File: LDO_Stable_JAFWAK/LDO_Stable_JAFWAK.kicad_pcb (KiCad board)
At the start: 4 copper layers, 96.5 x 50.8 mm, 76 parts, among them J1 VIN_DC, J12 EN_FG, J15 VOUT_BUFF, J16 VDD_SEL, J17 VS_BUFF, J18 EN_SEL, J2 VOUT, J24 Load Cell and Buffer, J3 GND, J4 GND, J5 EN_AIN_SEL, J6 AD_PINS, J8 VIN_FG, Q10 FDV305N, Q6 FDV305N, Q7 FDV305N, Q8 FDV305N, Q9 FDV305N, U1 SU272AFJK_LDO, U2 TMP235A2DBZR, U5 BUF634AIDR, U6 FXLP34, U7 BUF634AIDR, U8 FXLP34

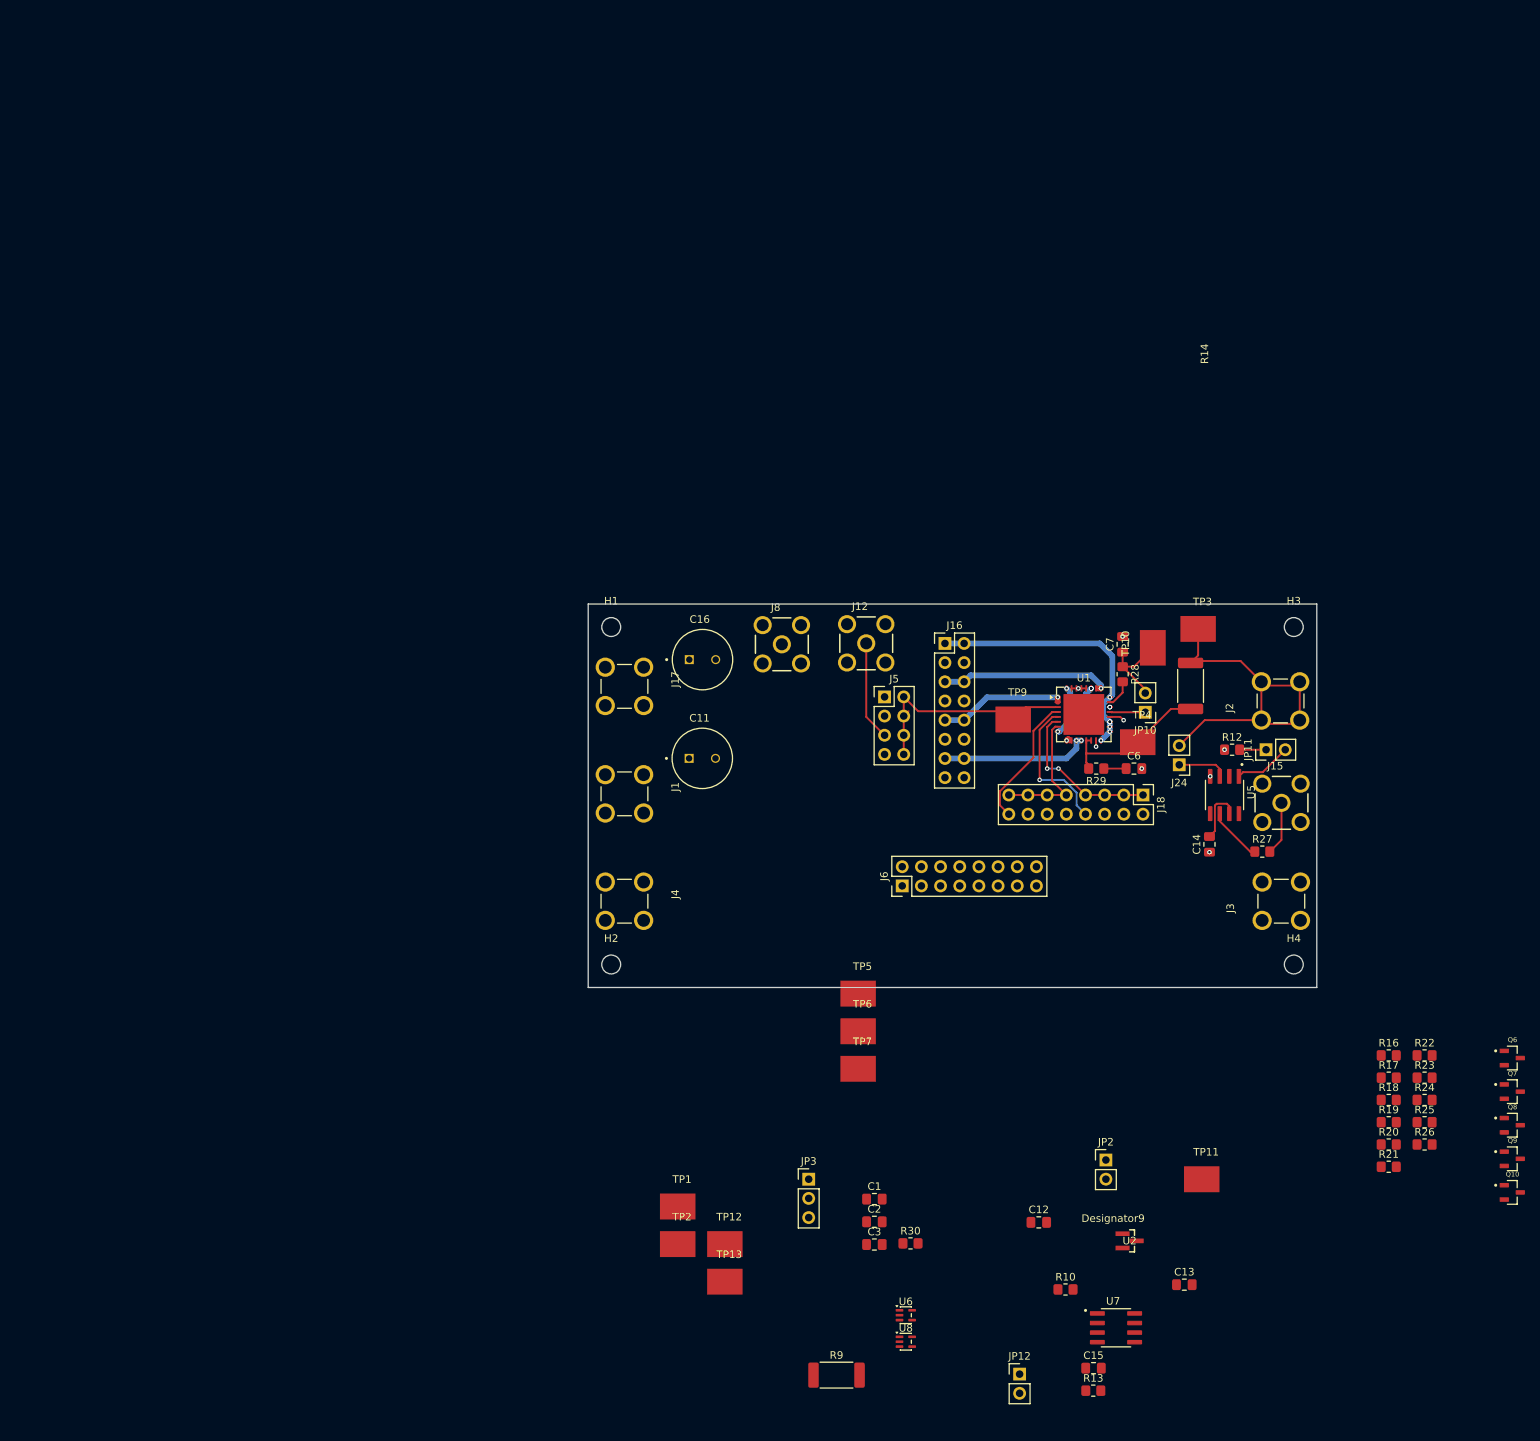
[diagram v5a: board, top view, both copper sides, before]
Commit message: Update PCB placement and routing
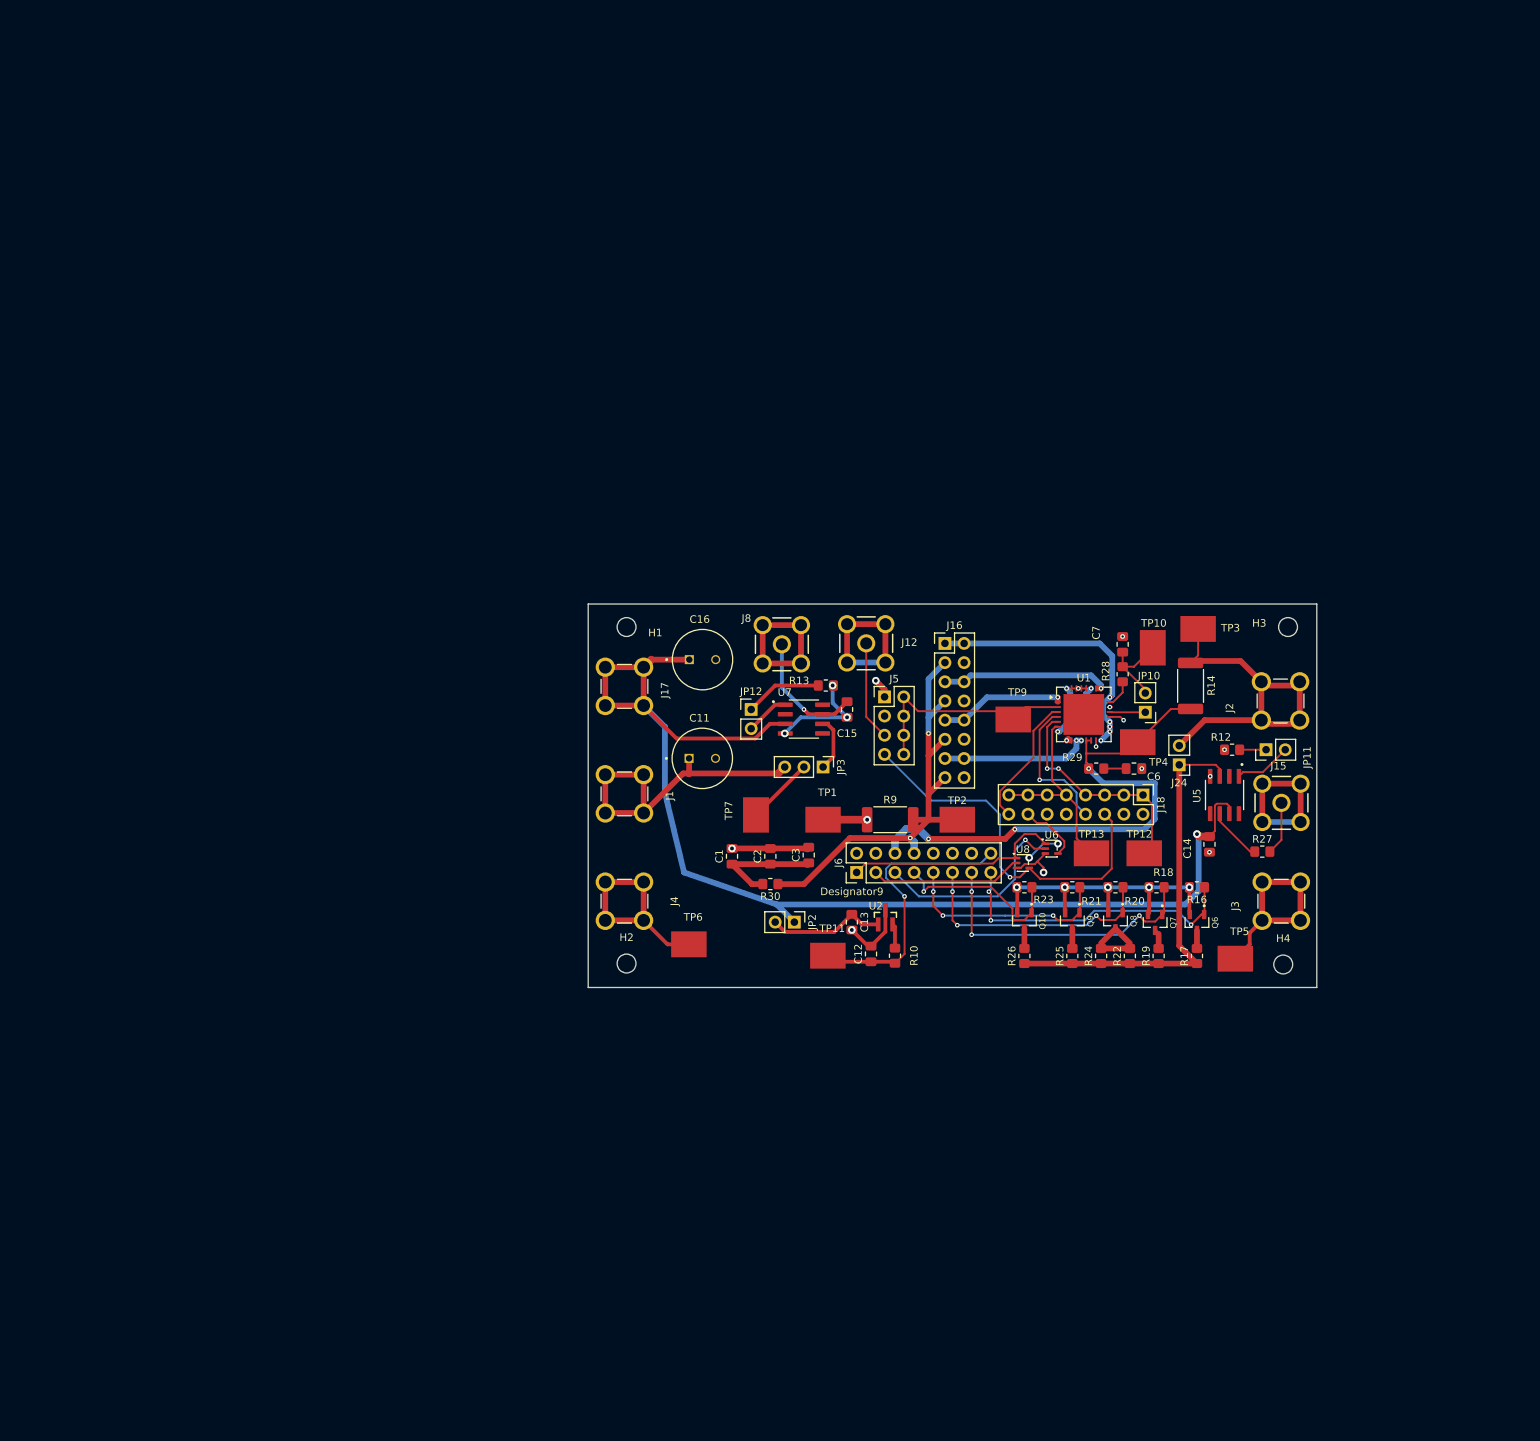
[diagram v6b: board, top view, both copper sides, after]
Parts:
- moved R13 99.9 mm to (107.7, 87.0), turned to 180 degrees
- moved JP12 95.0 mm to (97.8, 90.2)
- moved C15 93.2 mm to (110.5, 90.2), turned to 90 degrees
- moved U7 90.6 mm to (104.8, 91.4)
- moved TP12 75.9 mm to (149.9, 109.2)
- moved TP13 74.7 mm to (142.9, 109.2)
- moved Q10 74.0 mm to (134.0, 118.2), turned to -90 degrees
- moved R9 73.9 mm to (116.2, 104.8)
- moved TP2 67.3 mm to (125.1, 104.8)
- moved Q9 66.3 mm to (140.3, 118.2), turned to -90 degrees
- moved U8 65.3 mm to (133.8, 110.5)
- moved C13 65.2 mm to (111.1, 118.3), turned to -90 degrees
- moved U6 64.8 mm to (137.6, 108.6)
- moved Q8 59.1 mm to (146.1, 118.2), turned to -90 degrees
- moved R23 58.7 mm to (134.0, 113.7), turned to 180 degrees
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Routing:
- net GND: track 5.32 -> 201.9 mm, vias 18 -> 21
- net VS_BUFF: track 7.54 -> 161.6 mm, vias 0 -> 1
- net INB: track 0.00 -> 62.5 mm, vias 4 -> 2
- net OUTA: track 20.8 -> 73.5 mm, vias 0 -> 3
- net /LDO Harness/AD1_SHIFT: track 0.00 -> 50.5 mm, vias 0 -> 1
- net /Buffer/IN: track 6.58 -> 56.7 mm
- net Net-(J1-Pin_1): track 0.00 -> 43.5 mm
- net /B0: track 0.00 -> 40.3 mm, vias 0 -> 3
- net /B1: track 0.00 -> 39.0 mm, vias 0 -> 3
- net /TEMP: track 0.00 -> 38.1 mm, vias 0 -> 1
- net /B2: track 0.00 -> 33.7 mm, vias 0 -> 3
- net /ADV: track 0.00 -> 29.1 mm
- net /B3: track 0.00 -> 28.4 mm, vias 0 -> 3
- net /~{EN}: track 0.00 -> 27.0 mm, vias 0 -> 1
- net /B4: track 0.00 -> 24.0 mm, vias 0 -> 1
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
